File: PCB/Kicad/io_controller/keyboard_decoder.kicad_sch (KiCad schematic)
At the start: 8 parts, among them U25 74LS08, U26 74LS28, U27 74LS08, U28 74LS08, U29 74LS28, U30 74LS08, U31 AT28C256-15PU, U32 74LS377

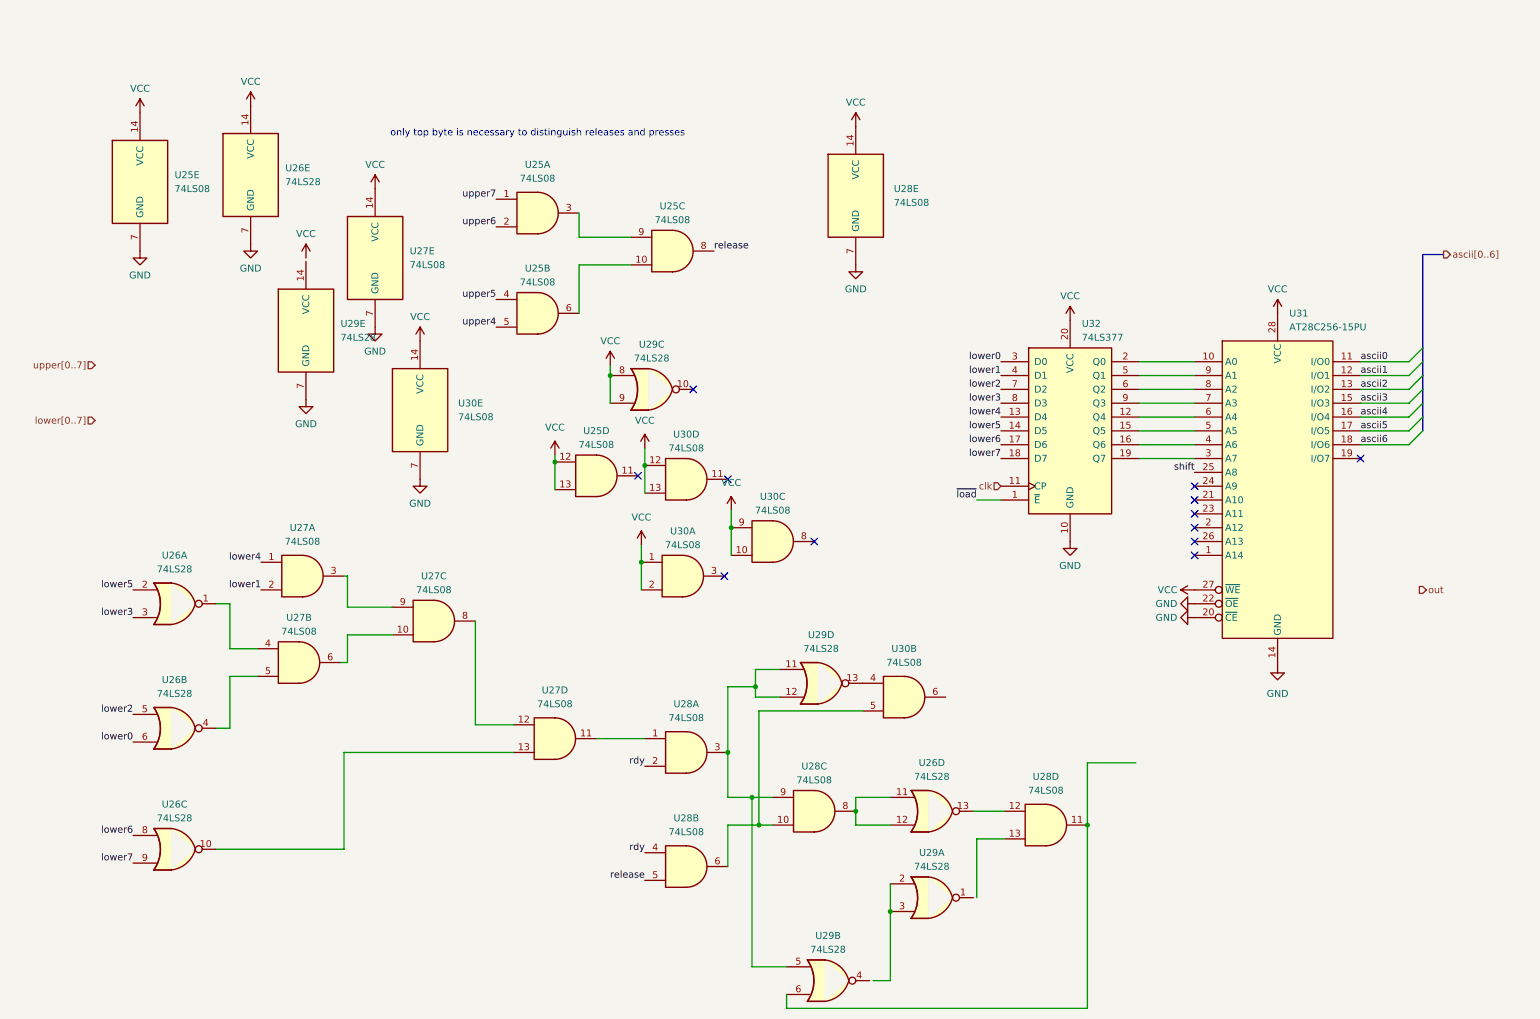
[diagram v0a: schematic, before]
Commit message: initial version of io controller schematic
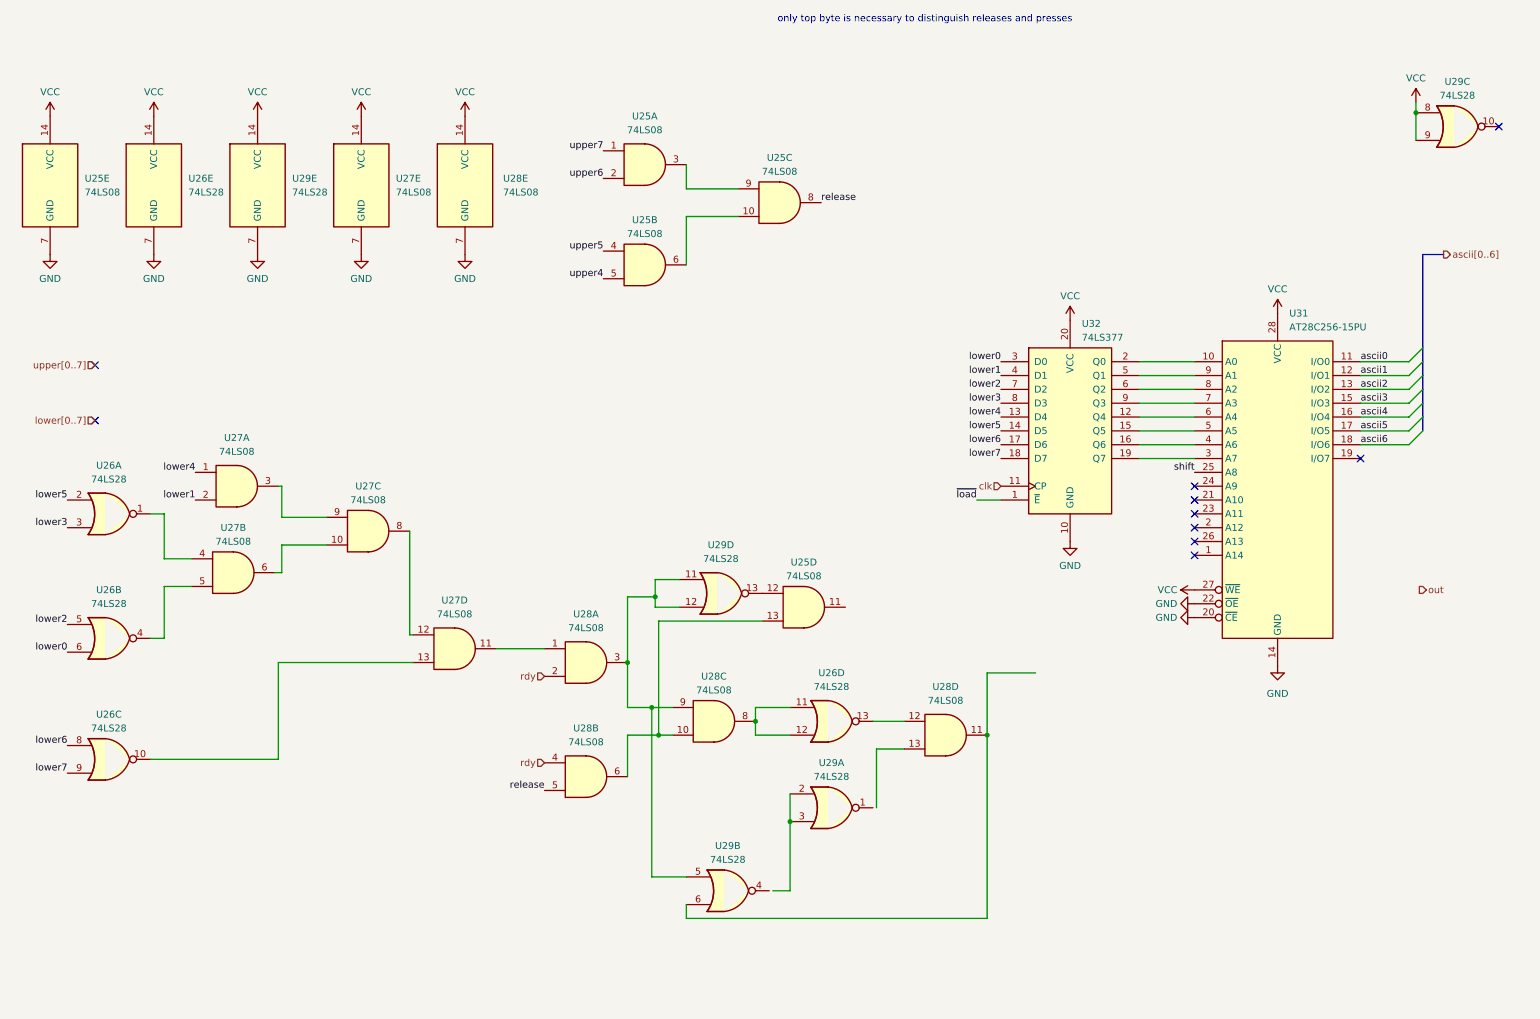
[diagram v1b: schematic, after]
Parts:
- removed U30: 74LS08, symbol 74xx:74LS08
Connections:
- net VCC: now also U29.14 (VCC); no longer U25.12, U25.13
- net at U28.10, U28.6: now also U25.13
- net at U29.13: now also U25.12
- no-connect marks 12 -> 10
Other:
- moved on the sheet: U25A, U25B, U25C, U25E, U26A, U26B, U26C, U26D, U26E, U27A, U27B, U27C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

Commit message: more spice models and bugfixes ; more tests of io_controller - mostly keyboard
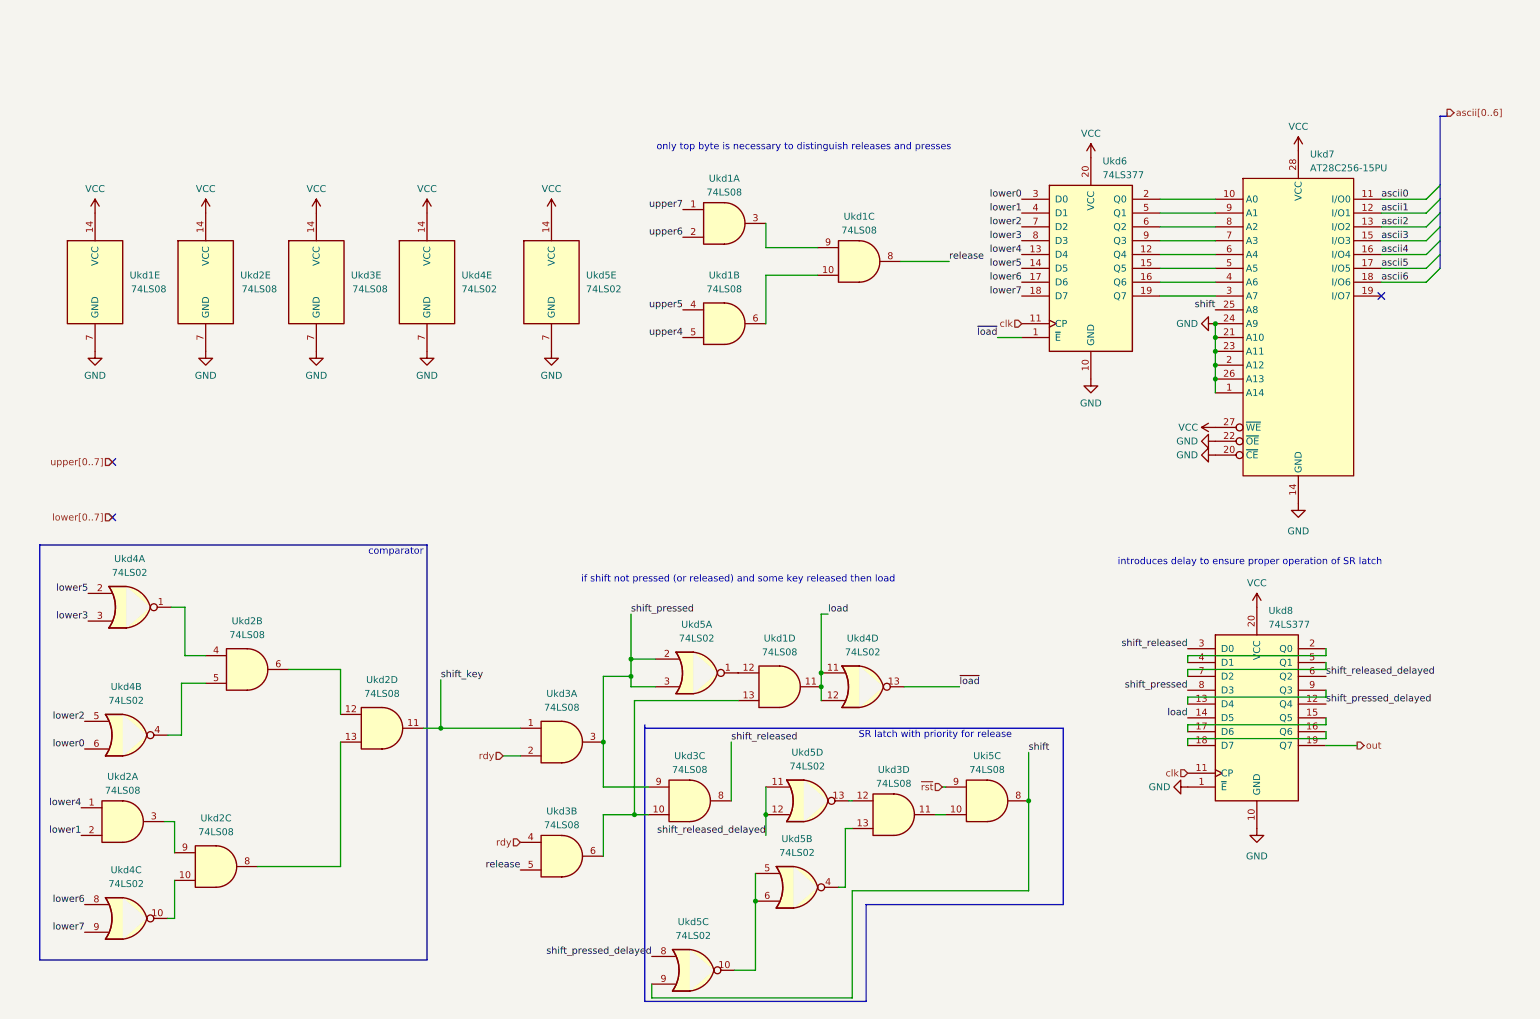
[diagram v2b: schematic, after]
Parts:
- removed U26, U29: 74LS28, symbol 74xx:74LS28
- removed unit 5 of U27
- removed unit 5 of U28
- added unit 5 of Ukd2
- added unit 5 of Ukd3
- added Ukd4, Ukd5: 74LS02, symbol 74xx:74LS02
- added Ukd8: 74LS377, symbol 74xx:74LS377
- added Uki5: 74LS08, symbol 74xx:74LS08
- renumbered U25 to Ukd1, U27 to Ukd2, U28 to Ukd3, U32 to Ukd6, U31 to Ukd7
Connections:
- net GND: now also Ukd7.1 (A14), Ukd7.2 (A12), Ukd7.21 (A10), Ukd7.23 (A11), Ukd7.24 (A9), Ukd7.26 (A13), Ukd2.7 (GND), Ukd3.7 (GND), Ukd4.7 (GND), Ukd5.7 (GND), Ukd8.1 (~{E}), Ukd8.10 (GND)
- net VCC: now also Ukd2.14 (VCC), Ukd3.14 (VCC), Ukd4.14 (VCC), Ukd5.14 (VCC), Ukd8.20 (VCC)
- net clk: now also Ukd8.11 (CP)
- net lower0: now also Ukd4.6
- net lower2: now also Ukd4.5
- net lower3: now also Ukd4.3
- net lower5: now also Ukd4.2
- net lower6: now also Ukd4.8
- net lower7: now also Ukd4.9
- net out: now also Ukd8.19 (Q7)
- net shift: now also Ukd5.9, Uki5.8
- net ~{load}: now also Ukd4.13
- net shift_key: now reaches Ukd2.11, Ukd3.1
- net at Ukd2.12: now also Ukd2.6; no longer Ukd2.8
- net at Ukd2.13: now also Ukd2.8
- net at Ukd2.4: now also Ukd4.1
- net at Ukd2.5: now also Ukd4.4
- net at Ukd2.10: now also Ukd4.10; no longer Ukd2.6
- net load: now reaches Ukd1.11
- net load: now also Ukd4.11, Ukd4.12, Ukd8.14 (D5)
- net at Ukd1.12: now also Ukd5.1
- net shift_released: now reaches Ukd3.8
- net shift_released: now also Ukd8.3 (D0)
- net shift_pressed: now reaches Ukd3.3, Ukd3.9
- net shift_pressed: now also Ukd5.2, Ukd5.3, Ukd8.8 (D3)
- net at Ukd3.12: now also Ukd5.13
- net at Ukd3.11: now also Uki5.10
- net at Ukd3.13: now also Ukd5.4
- new net: Ukd5.10, Ukd5.5, Ukd5.6
- new net: Ukd8.13 (D4), Ukd8.9 (Q3)
- new net: Ukd8.15 (Q5), Ukd8.17 (D6)
- new net: Ukd8.16 (Q6), Ukd8.18 (D7)
- new net: Ukd8.2 (Q0), Ukd8.4 (D1)
- new net: Ukd8.5 (Q1), Ukd8.7 (D2)
- new net shift_pressed_delayed: Ukd5.8, Ukd8.12 (Q4)
- new net shift_released_delayed: Ukd5.11, Ukd5.12, Ukd8.6 (Q2)
- new net ~{rst}: Uki5.9
- no-connect marks 10 -> 3
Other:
- note added: "SR latch with priority for release"
- note added: "comparator"
- note added: "if shift not pressed (or released) and some key released then load"
- note added: "introduces delay to ensure proper operation of SR latch"
- company: (none) -> AGH Logic Unit
- title: (none) -> Keyboard Decoder
- moved on the sheet: Ukd1A, Ukd1B, Ukd1C, Ukd1D, Ukd1E, Ukd2A, Ukd2B, Ukd2C, Ukd2D, Ukd3A, Ukd3B, Ukd3C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

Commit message: primarily keyboard decoder finish ; preliminary layout
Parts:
- added Ckd1, Ckd2, Ckd3, Ckd4, Ckd5, Ckd6, Ckd7, Ckd8: 0.1u, Capacitor_SMD:C_0402_1005Metric, symbol Device:C
- Ukd1, Ukd2, Ukd3, Ukd4, Ukd5, Uki5: footprint (none) -> Package_SO:SOIC-14_3.9x8.7mm_P1.27mm
- Ukd6, Ukd8: footprint (none) -> Package_SO:SSOP-20_5.3x7.2mm_P0.65mm
- Ukd7: footprint (none) -> Package_DIP:DIP-28_W15.24mm_Socket
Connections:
- net GND: now also Ckd1.2, Ckd2.2, Ckd3.2, Ckd4.2, Ckd5.2, Ckd6.2, Ckd7.2, Ckd8.2
- net VCC: now also Ckd1.1, Ckd2.1, Ckd3.1, Ckd4.1, Ckd5.1, Ckd6.1, Ckd7.1, Ckd8.1

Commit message: io controller update
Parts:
- Ckd1, Ckd2, Ckd3, Ckd4, Ckd5, Ckd6, Ckd7, Ckd8: value 0.1u -> 100nF
- Ukd1, Ukd2, Ukd3, Uki5: value 74LS08 -> 7408; footprint Package_SO:SOIC-14_3.9x8.7mm_P1.27mm -> Package_SO:SO-14_3.9x8.65mm_P1.27mm
- Ukd4, Ukd5: value 74LS02 -> 7402
- Ukd6, Ukd8: value 74LS377 -> 74377
- Ukd7: now not fitted

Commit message: Forgot to add few things
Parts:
- Ukd4, Ukd5: footprint Package_SO:SOIC-14_3.9x8.7mm_P1.27mm -> Package_SO:SO-14_3.9x8.65mm_P1.27mm
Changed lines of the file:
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@@
 			)
 		)
-		(property "Footprint" "Package_SO:SOIC-14_3.9x8.7mm_P1.27mm"
+		(property "Footprint" "Package_SO:SO-14_3.9x8.65mm_P1.27mm"
 			(at 31.75 167.64 0)
 			(hide yes)
@@
 			)
 		)
-		(property "Datasheet" "http://www.ti.com/lit/gpn/sn74ls02"
+		(property "Datasheet" "https://www.tme.eu/pl/en/details/sn74hc02dr/gates-inverters/texas-instruments/"
 			(at 31.75 167.64 0)
 			(hide yes)
@@
 			)
 		)
-		(property "Footprint" "Package_SO:SOIC-14_3.9x8.7mm_P1.27mm"
+		(property "Footprint" "Package_SO:SO-14_3.9x8.65mm_P1.27mm"
 			(at 135.89 177.165 0)
 			(hide yes)
@@
 			)
 		)
-		(property "Datasheet" "http://www.ti.com/lit/gpn/sn74ls02"
+		(property "Datasheet" "https://www.tme.eu/pl/en/details/sn74hc02dr/gates-inverters/texas-instruments/"
 			(at 135.89 177.165 0)
 			(hide yes)
@@
 			)
 		)
-		(property "Footprint" "Package_SO:SOIC-14_3.9x8.7mm_P1.27mm"
+		(property "Footprint" "Package_SO:SO-14_3.9x8.65mm_P1.27mm"
 			(at 86.995 50.8 0)
 			(hide yes)
@@
 			)
 		)
-		(property "Datasheet" "https://www.tme.eu/pl/details/74hc02d.653/bramki-inwertery/nexperia/74hc02d-653/"
+		(property "Datasheet" "https://www.tme.eu/pl/en/details/sn74hc02dr/gates-inverters/texas-instruments/"
 			(at 86.995 50.8 0)
 			(hide yes)
@@
 			)
 		)
-		(property "Footprint" "Package_SO:SOIC-14_3.9x8.7mm_P1.27mm"
+		(property "Footprint" "Package_SO:SO-14_3.9x8.65mm_P1.27mm"
 			(at 31.75 133.985 0)
 			(hide yes)
@@
 			)
 		)
-		(property "Datasheet" "http://www.ti.com/lit/gpn/sn74ls02"
+		(property "Datasheet" "https://www.tme.eu/pl/en/details/sn74hc02dr/gates-inverters/texas-instruments/"
 			(at 31.75 133.985 0)
 			(hide yes)
@@
 			)
 		)
-		(property "Footprint" "Package_SO:SOIC-14_3.9x8.7mm_P1.27mm"
+		(property "Footprint" "Package_SO:SO-14_3.9x8.65mm_P1.27mm"
 			(at 136.525 122.555 0)
 			(hide yes)
@@
 			)
 		)
-		(property "Datasheet" "http://www.ti.com/lit/gpn/sn74ls02"
+		(property "Datasheet" "https://www.tme.eu/pl/en/details/sn74hc02dr/gates-inverters/texas-instruments/"
 			(at 136.525 122.555 0)
 			(hide yes)
@@
 			)
 		)
-		(property "Footprint" "Package_SO:SOIC-14_3.9x8.7mm_P1.27mm"
+		(property "Footprint" "Package_SO:SO-14_3.9x8.65mm_P1.27mm"
 			(at 109.855 50.8 0)
 			(hide yes)
@@
 			)
 		)
-		(property "Datasheet" "https://www.tme.eu/pl/details/74hc02d.653/bramki-inwertery/nexperia/74hc02d-653/"
+		(property "Datasheet" "https://www.tme.eu/pl/en/details/sn74hc02dr/gates-inverters/texas-instruments/"
 			(at 109.855 50.8 0)
 			(hide yes)
@@
 			)
 		)
-		(property "Footprint" "Package_SO:SOIC-14_3.9x8.7mm_P1.27mm"
+		(property "Footprint" "Package_SO:SO-14_3.9x8.65mm_P1.27mm"
 			(at 32.385 110.49 0)
 			(hide yes)
@@
 			)
 		)
-		(property "Datasheet" "http://www.ti.com/lit/gpn/sn74ls02"
+		(property "Datasheet" "https://www.tme.eu/pl/en/details/sn74hc02dr/gates-inverters/texas-instruments/"
 			(at 32.385 110.49 0)
 			(hide yes)
@@
 			)
 		)
-		(property "Footprint" "Package_SO:SOIC-14_3.9x8.7mm_P1.27mm"
+		(property "Footprint" "Package_SO:SO-14_3.9x8.65mm_P1.27mm"
 			(at 154.94 161.925 0)
 			(hide yes)
@@
 			)
 		)
-		(property "Datasheet" "http://www.ti.com/lit/gpn/sn74ls02"
+		(property "Datasheet" "https://www.tme.eu/pl/en/details/sn74hc02dr/gates-inverters/texas-instruments/"
 			(at 154.94 161.925 0)
 			(hide yes)
@@
 			)
 		)
-		(property "Footprint" "Package_SO:SOIC-14_3.9x8.7mm_P1.27mm"
+		(property "Footprint" "Package_SO:SO-14_3.9x8.65mm_P1.27mm"
 			(at 156.845 146.05 0)
 			(hide yes)
@@
 			)
 		)
-		(property "Datasheet" "http://www.ti.com/lit/gpn/sn74ls02"
+		(property "Datasheet" "https://www.tme.eu/pl/en/details/sn74hc02dr/gates-inverters/texas-instruments/"
 			(at 156.845 146.05 0)
 			(hide yes)
@@
 			)
 		)
-		(property "Footprint" "Package_SO:SOIC-14_3.9x8.7mm_P1.27mm"
+		(property "Footprint" "Package_SO:SO-14_3.9x8.65mm_P1.27mm"
 			(at 167.005 125.095 0)
 			(hide yes)
@@
 			)
 		)
-		(property "Datasheet" "http://www.ti.com/lit/gpn/sn74ls02"
+		(property "Datasheet" "https://www.tme.eu/pl/en/details/sn74hc02dr/gates-inverters/texas-instruments/"
 			(at 167.005 125.095 0)
 			(hide yes)
